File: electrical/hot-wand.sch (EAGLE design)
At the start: 203 parts, among them IC1 12V R-78K12-2.0, IC2 3V3 R-78K3.3, Q1 STP19NF20, Q2 IRF510, Q3 BC846B, Q4 SIS862ADN-T1-GE3, Q5 SIS862ADN-T1-GE3, Q6 DMTH64M2LPDWQ-13, Q7 SIS862ADN-T1-GE3, Q8 2N7002K, Q9 G3404, SW1 SW-TACT-SIDE, U1 TPS54560DDA, U2 1EDN8511BXUSA1, U3 STM32F030F4P6, U4 SSD1306-4PIN-0.91N-VERT, U5 INA138, U6 LM74810QDRRRQ1, U7 AP53781, Y1 27.12 MHz 10pF

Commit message: shopping list wip
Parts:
- VR2, VR3: PARTNUM TC33X-1-102E -> TC33X-2-102E
- VR4: PARTNUM TC33X-1-472E -> TC33X-2-472E
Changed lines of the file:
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@@
 <part name="VR2" library="hot-wand" deviceset="POT" device="-35WR1KLFTR_V3" value="1K">
 <attribute name="JLC-DNP" value="1"/>
-<attribute name="PARTNUM" value="TC33X-1-102E"/>
+<attribute name="PARTNUM" value="TC33X-2-102E"/>
 </part>
 <part name="C58" library="hot-wand" deviceset="CAP" device="0603-CAP" value="3n3">
@@
 <part name="VR4" library="hot-wand" deviceset="POT" device="-35WR1KLFTR_V2" value="4K7">
 <attribute name="JLC-DNP" value="1"/>
-<attribute name="PARTNUM" value="TC33X-1-472E"/>
+<attribute name="PARTNUM" value="TC33X-2-472E"/>
 </part>
 <part name="SJ2" library="hot-wand" deviceset="SOLDERJUMPER" device="NO" value="">
@@
 <part name="VR3" library="hot-wand" deviceset="POT" device="-35WR1KLFTR_V3" value="1K">
 <attribute name="JLC-DNP" value="1"/>
-<attribute name="PARTNUM" value="TC33X-1-102E"/>
+<attribute name="PARTNUM" value="TC33X-2-102E"/>
 </part>
 <part name="R32" library="hot-wand" deviceset="RESISTOR" device="0805-RES" value="100Ω">

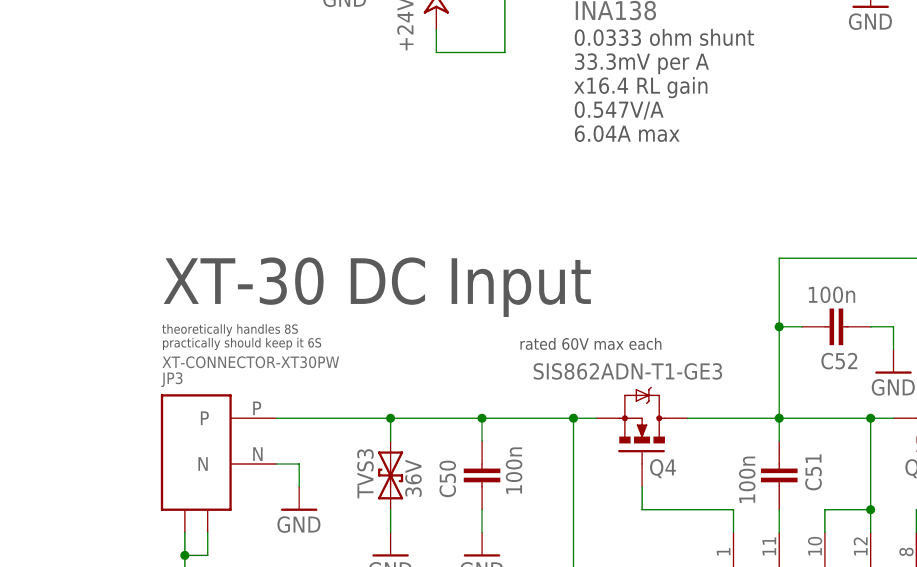
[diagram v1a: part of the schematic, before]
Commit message: XT-30 to XT30
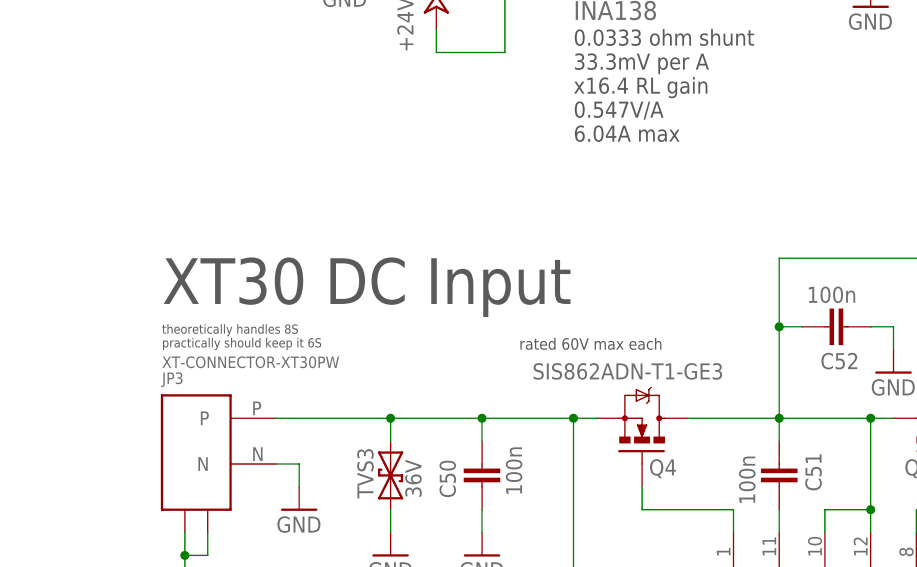
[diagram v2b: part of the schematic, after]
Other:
- note added: "XT30 DC Input"
- note removed: "XT-30 DC Input"
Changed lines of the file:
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@@
 <text x="259.08" y="-251.46" size="1.016" layer="96" align="bottom-right">Bourns 5300-17-RC</text>
 <text x="156.21" y="-721.868" size="1.778" layer="97" rot="R270" align="bottom-right">select 20V</text>
-<text x="27.94" y="-566.42" size="5.08" layer="97">XT-30 DC Input</text>
+<text x="27.94" y="-566.42" size="5.08" layer="97">XT30 DC Input</text>
 <text x="25.4" y="-685.8" size="5.08" layer="97">USB-PD Input</text>
 <text x="31.496" y="-644.144" size="1.016" layer="97" rot="R90" align="bottom-right">gate rated 20V

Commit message: updated an invalid potentiometer part
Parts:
- VR4: value 4K7 -> 5K; PARTNUM TC33X-2-472E -> TC33X-2-502
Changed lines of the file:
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@@
 <attribute name="JLC-DNP" value="1"/>
 </part>
-<part name="VR4" library="hot-wand" deviceset="POT" device="-35WR1KLFTR_V2" value="4K7">
+<part name="VR4" library="hot-wand" deviceset="POT" device="-35WR1KLFTR_V2" value="5K">
 <attribute name="JLC-DNP" value="1"/>
-<attribute name="PARTNUM" value="TC33X-2-472E"/>
+<attribute name="PARTNUM" value="TC33X-2-502"/>
 </part>
 <part name="SJ2" library="hot-wand" deviceset="SOLDERJUMPER" device="NO" value="">

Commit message: lite design order
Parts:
- C13, C14, C15, C16, C17, C18, C19, C26, C33, C39, C40: JLC-DNP 2 -> (none)
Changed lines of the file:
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@@
 </part>
 <part name="C33" library="hot-wand" deviceset="CAP" device="0805" value="10pF 500V">
-<attribute name="JLC-DNP" value="2"/>
 <attribute name="JLCPARTNUM" value="C6629873"/>
 <attribute name="PARTNUM" value="QCCT102Q100J1GV001E"/>
@@
 <part name="GND11" library="hot-wand" deviceset="GND" device=""/>
 <part name="C26" library="hot-wand" deviceset="CAP" device="0805" value="100pF 1000V">
-<attribute name="JLC-DNP" value="2"/>
 <attribute name="JLCPARTNUM" value="C6958299"/>
 </part>
@@
 <part name="C19" library="hot-wand" deviceset="CAP" device="0805" value="DNP">
 <attribute name="DNP" value="1"/>
-<attribute name="JLC-DNP" value="2"/>
 <attribute name="JLCPARTNUM" value="C6958299"/>
 </part>
 <part name="C18" library="hot-wand" deviceset="CAP" device="0805" value="100pF 1000V">
-<attribute name="JLC-DNP" value="2"/>
 <attribute name="JLCPARTNUM" value="C6958299"/>
 </part>
 <part name="C17" library="hot-wand" deviceset="CAP" device="0805" value="100pF 1000V">
-<attribute name="JLC-DNP" value="2"/>
 <attribute name="JLCPARTNUM" value="C6958299"/>
 </part>
 <part name="C16" library="hot-wand" deviceset="CAP" device="0805" value="100pF 1000V">
-<attribute name="JLC-DNP" value="2"/>
 <attribute name="JLCPARTNUM" value="C6958299"/>
 </part>
 <part name="C15" library="hot-wand" deviceset="CAP" device="0805" value="100pF 1000V">
-<attribute name="JLC-DNP" value="2"/>
 <attribute name="JLCPARTNUM" value="C6958299"/>
 </part>
 <part name="C14" library="hot-wand" deviceset="CAP" device="0805" value="100pF 1000V">
-<attribute name="JLC-DNP" value="2"/>
 <attribute name="JLCPARTNUM" value="C6958299"/>
 </part>
 <part name="C13" library="hot-wand" deviceset="CAP" device="0805" value="100pF 1000V">
-<attribute name="JLC-DNP" value="2"/>
 <attribute name="JLCPARTNUM" value="C6958299"/>
 <attribute name="PARTNUM" value="QCCT102Q101J1GV001E"/>
@@
 </part>
 <part name="C39" library="hot-wand" deviceset="CAP" device="0805" value="100pF">
-<attribute name="JLC-DNP" value="2"/>
 <attribute name="JLCPARTNUM" value="C6958299"/>
 </part>
 <part name="C40" library="hot-wand" deviceset="CAP" device="0805" value="100pF">
-<attribute name="JLC-DNP" value="2"/>
-<attribute name="JLCPARTNUM" value="C6958299"/>
-</part>
+<attribute name="JLCPARTNUM" value="C6958299"/>
+</part>

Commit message: 13.56 MHz design files for ordering
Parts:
- R10: JLCPARTNUM (none) -> C22775
- R14, R52: device hot-wand:RESISTOR0805-RES -> hot-wand:RESISTOR0603-RES; JLCPARTNUM C441975 -> C22775
- TVS6: JLCPARTNUM (none) -> C148223; JLCPCBPART C148223 -> (none)

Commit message: out of stock part number change
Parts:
- L9: PARTNUM 5300-17-RC -> AIAP-01-220K-T
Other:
- note added: "AIAP-01-220K-T"
- note removed: "Bourns 5300-17-RC"
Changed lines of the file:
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@@
 <grid distance="0.1" unitdist="inch" unit="inch" style="lines" multiple="1" display="no" altdistance="0.01" altunitdist="inch" altunit="inch"/>
 <layers>
-<layer number="1" name="Top" color="4" fill="1" visible="yes" active="no"/>
-<layer number="2" name="Route2" color="1" fill="3" visible="yes" active="no"/>
-<layer number="3" name="Route3" color="4" fill="3" visible="yes" active="no"/>
-<layer number="4" name="Route4" color="1" fill="4" visible="yes" active="no"/>
-<layer number="5" name="Route5" color="4" fill="4" visible="yes" active="no"/>
-<layer number="6" name="Route6" color="1" fill="8" visible="yes" active="no"/>
-<layer number="7" name="Route7" color="4" fill="8" visible="yes" active="no"/>
-<layer number="8" name="Route8" color="1" fill="2" visible="yes" active="no"/>
-<layer number="9" name="Route9" color="4" fill="2" visible="yes" active="no"/>
-<layer number="10" name="Route10" color="1" fill="7" visible="yes" active="no"/>
-<layer number="11" name="Route11" color="4" fill="7" visible="yes" active="no"/>
-<layer number="12" name="Route12" color="1" fill="5" visible="yes" active="no"/>
-<layer number="13" name="Route13" color="4" fill="5" visible="yes" active="no"/>
-<layer number="14" name="Route14" color="1" fill="6" visible="yes" active="no"/>
-<layer number="15" name="Route15" color="4" fill="6" visible="yes" active="no"/>
-<layer number="16" name="Bottom" color="1" fill="1" visible="yes" active="no"/>
-<layer number="17" name="Pads" color="2" fill="1" visible="yes" active="no"/>
-<layer number="18" name="Vias" color="2" fill="1" visible="yes" active="no"/>
-<layer number="19" name="Unrouted" color="6" fill="1" visible="yes" active="no"/>
-<layer number="20" name="Dimension" color="15" fill="1" visible="yes" active="no"/>
-<layer number="21" name="tPlace" color="7" fill="1" visible="yes" active="no"/>
-<layer number="22" name="bPlace" color="7" fill="1" visible="yes" active="no"/>
-<layer number="23" name="tOrigins" color="15" fill="1" visible="yes" active="no"/>
-<layer number="24" name="bOrigins" color="15" fill="1" visible="yes" active="no"/>
-<layer number="25" name="tNames" color="7" fill="1" visible="yes" active="no"/>
-<layer number="26" name="bNames" color="7" fill="1" visible="yes" active="no"/>
-<layer number="27" name="tValues" color="7" fill="1" visible="yes" active="no"/>
-<layer number="28" name="bValues" color="7" fill="1" visible="yes" active="no"/>
+<layer number="1" name="Top" color="4" fill="1" visible="no" active="no"/>
+<layer number="2" name="Route2" color="1" fill="3" visible="no" active="no"/>
+<layer number="3" name="Route3" color="4" fill="3" visible="no" active="no"/>
+<layer number="4" name="Route4" color="1" fill="4" visible="no" active="no"/>
+<layer number="5" name="Route5" color="4" fill="4" visible="no" active="no"/>
+<layer number="6" name="Route6" color="1" fill="8" visible="no" active="no"/>
+<layer number="7" name="Route7" color="4" fill="8" visible="no" active="no"/>
+<layer number="8" name="Route8" color="1" fill="2" visible="no" active="no"/>
+<layer number="9" name="Route9" color="4" fill="2" visible="no" active="no"/>
+<layer number="10" name="Route10" color="1" fill="7" visible="no" active="no"/>
+<layer number="11" name="Route11" color="4" fill="7" visible="no" active="no"/>
+<layer number="12" name="Route12" color="1" fill="5" visible="no" active="no"/>
+<layer number="13" name="Route13" color="4" fill="5" visible="no" active="no"/>
+<layer number="14" name="Route14" color="1" fill="6" visible="no" active="no"/>
+<layer number="15" name="Route15" color="4" fill="6" visible="no" active="no"/>
+<layer number="16" name="Bottom" color="1" fill="1" visible="no" active="no"/>
+<layer number="17" name="Pads" color="2" fill="1" visible="no" active="no"/>
+<layer number="18" name="Vias" color="2" fill="1" visible="no" active="no"/>
+<layer number="19" name="Unrouted" color="6" fill="1" visible="no" active="no"/>
+<layer number="20" name="Dimension" color="15" fill="1" visible="no" active="no"/>
+<layer number="21" name="tPlace" color="7" fill="1" visible="no" active="no"/>
+<layer number="22" name="bPlace" color="7" fill="1" visible="no" active="no"/>
+<layer number="23" name="tOrigins" color="15" fill="1" visible="no" active="no"/>
+<layer number="24" name="bOrigins" color="15" fill="1" visible="no" active="no"/>
+<layer number="25" name="tNames" color="7" fill="1" visible="no" active="no"/>
+<layer number="26" name="bNames" color="7" fill="1" visible="no" active="no"/>
+<layer number="27" name="tValues" color="7" fill="1" visible="no" active="no"/>
+<layer number="28" name="bValues" color="7" fill="1" visible="no" active="no"/>
 <layer number="29" name="tStop" color="7" fill="3" visible="no" active="no"/>
 <layer number="30" name="bStop" color="7" fill="6" visible="no" active="no"/>
@@
 <layer number="35" name="tGlue" color="7" fill="4" visible="no" active="no"/>
 <layer number="36" name="bGlue" color="7" fill="5" visible="no" active="no"/>
-<layer number="37" name="tTest" color="7" fill="1" visible="yes" active="no"/>
-<layer number="38" name="bTest" color="7" fill="1" visible="yes" active="no"/>
+<layer number="37" name="tTest" color="7" fill="1" visible="no" active="no"/>
+<layer number="38" name="bTest" color="7" fill="1" visible="no" active="no"/>
 <layer number="39" name="tKeepout" color="4" fill="11" visible="no" active="no"/>
 <layer number="40" name="bKeepout" color="1" fill="11" visible="no" active="no"/>
@@
 <layer number="44" name="Drills" color="7" fill="1" visible="no" active="no"/>
 <layer number="45" name="Holes" color="7" fill="1" visible="no" active="no"/>
-<layer number="46" name="Milling" color="3" fill="1" visible="yes" active="no"/>
-<layer number="47" name="Measures" color="7" fill="1" visible="yes" active="no"/>
-<layer number="48" name="Document" color="7" fill="1" visible="yes" active="no"/>
-<layer number="49" name="Reference" color="7" fill="1" visible="yes" active="no"/>
-<layer number="50" name="dxf" color="7" fill="1" visible="yes" active="no"/>
-<layer number="51" name="tDocu" color="7" fill="1" visible="yes" active="no"/>
-<layer number="52" name="bDocu" color="7" fill="1" visible="yes" active="no"/>
-<layer number="53" name="tGND_GNDA" color="7" fill="9" visible="yes" active="no"/>
-<layer number="54" name="bGND_GNDA" color="1" fill="9" visible="yes" active="no"/>
-<layer number="56" name="wert" color="7" fill="1" visible="yes" active="no"/>
+<layer number="46" name="Milling" color="3" fill="1" visible="no" active="no"/>
+<layer number="47" name="Measures" color="7" fill="1" visible="no" active="no"/>
+<layer number="48" name="Document" color="7" fill="1" visible="no" active="no"/>
+<layer number="49" name="Reference" color="7" fill="1" visible="no" active="no"/>
+<layer number="50" name="dxf" color="7" fill="1" visible="no" active="no"/>
+<layer number="51" name="tDocu" color="7" fill="1" visible="no" active="no"/>
+<layer number="52" name="bDocu" color="7" fill="1" visible="no" active="no"/>
+<layer number="53" name="tGND_GNDA" color="7" fill="9" visible="no" active="no"/>
+<layer number="54" name="bGND_GNDA" color="1" fill="9" visible="no" active="no"/>
+<layer number="56" name="wert" color="7" fill="1" visible="no" active="no"/>
 <layer number="90" name="Modules" color="5" fill="1" visible="yes" active="yes"/>
 <layer number="91" name="Nets" color="2" fill="1" visible="yes" active="yes"/>
@@
 <part name="L9" library="hot-wand" deviceset="L-US" device="TFI0410" value="22uH">
 <attribute name="JLC-DNP" value="1"/>
-<attribute name="PARTNUM" value="5300-17-RC"/>
+<attribute name="PARTNUM" value="AIAP-01-220K-T"/>
 </part>
 <part name="C42" library="hot-wand" deviceset="CAP" device="0603-CAP" value="33nF">
@@
 <text x="64.77" y="-179.832" size="1.016" layer="97" rot="R270" align="bottom-right">200VDS 15A 20VGS
 0.11 Rdson</text>
-<text x="259.08" y="-251.46" size="1.016" layer="96" align="bottom-right">Bourns 5300-17-RC</text>
+<text x="259.08" y="-251.46" size="1.016" layer="96" align="bottom-right">AIAP-01-220K-T</text>
 <text x="156.21" y="-721.868" size="1.778" layer="97" rot="R270" align="bottom-right">select 20V</text>
 <text x="27.94" y="-566.42" size="5.08" layer="97">XT30 DC Input</text>

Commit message: new part number for small mosfet to lower costs
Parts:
- Q8: JLCPARTNUM C5224211;C54347659 -> C14498;C547263;C5224211;C54347659; PARTNUM 2N7002K;SSM3K388R,LF -> 2N7002K;SSM3K388R,LF;Si2318CDS-T1-GE3;PMV60ENEAR
- Q9: JLCPARTNUM C96615 -> C14498;C547263;C96615; PARTNUM G3404;MMFTN3404A;PJA3404A -> G3404;MMFTN3404A;PJA3404A;Si2318CDS-T1-GE3;PMV60ENEAR
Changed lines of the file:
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@@
 </part>
 <part name="Q8" library="hot-wand" deviceset="MOSFET-NCHANNEL" device="SMD" value="2N7002K">
-<attribute name="JLCPARTNUM" value="C5224211;C54347659"/>
-<attribute name="PARTNUM" value="2N7002K;SSM3K388R,LF"/>
+<attribute name="JLCPARTNUM" value="C14498;C547263;C5224211;C54347659"/>
+<attribute name="PARTNUM" value="2N7002K;SSM3K388R,LF;Si2318CDS-T1-GE3;PMV60ENEAR"/>
 </part>
 <part name="GND39" library="hot-wand" deviceset="GND" device=""/>
@@
 </part>
 <part name="Q9" library="hot-wand" deviceset="MOSFET-NCHANNEL" device="SMD" value="G3404">
-<attribute name="JLCPARTNUM" value="C96615"/>
-<attribute name="PARTNUM" value="G3404;MMFTN3404A;PJA3404A"/>
+<attribute name="JLCPARTNUM" value="C14498;C547263;C96615"/>
+<attribute name="PARTNUM" value="G3404;MMFTN3404A;PJA3404A;Si2318CDS-T1-GE3;PMV60ENEAR"/>
 </part>
 <part name="R44" library="hot-wand" deviceset="RESISTOR" device="0603-RES" value="4K7">

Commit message: thermistor part number change
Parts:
- THERM1, THERM2: PARTNUM BN35-3T103FB-100 -> B57891M0103K000
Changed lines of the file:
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@@
 <part name="THERM1" library="hot-wand" deviceset="THERMISTOR-NTC" device="-TH-2MM" value="10K/~3950">
 <attribute name="JLC-DNP" value="1"/>
-<attribute name="PARTNUM" value="BN35-3T103FB-100"/>
+<attribute name="PARTNUM" value="B57891M0103K000"/>
 </part>
 <part name="THERM2" library="hot-wand" deviceset="THERMISTOR-NTC" device="-TH-2MM" value="10K/~3950">
 <attribute name="JLC-DNP" value="1"/>
-<attribute name="PARTNUM" value="BN35-3T103FB-100"/>
+<attribute name="PARTNUM" value="B57891M0103K000"/>
 </part>
 <part name="GND58" library="hot-wand" deviceset="GND" device=""/>
